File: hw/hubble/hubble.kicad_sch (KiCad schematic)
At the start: 36 parts

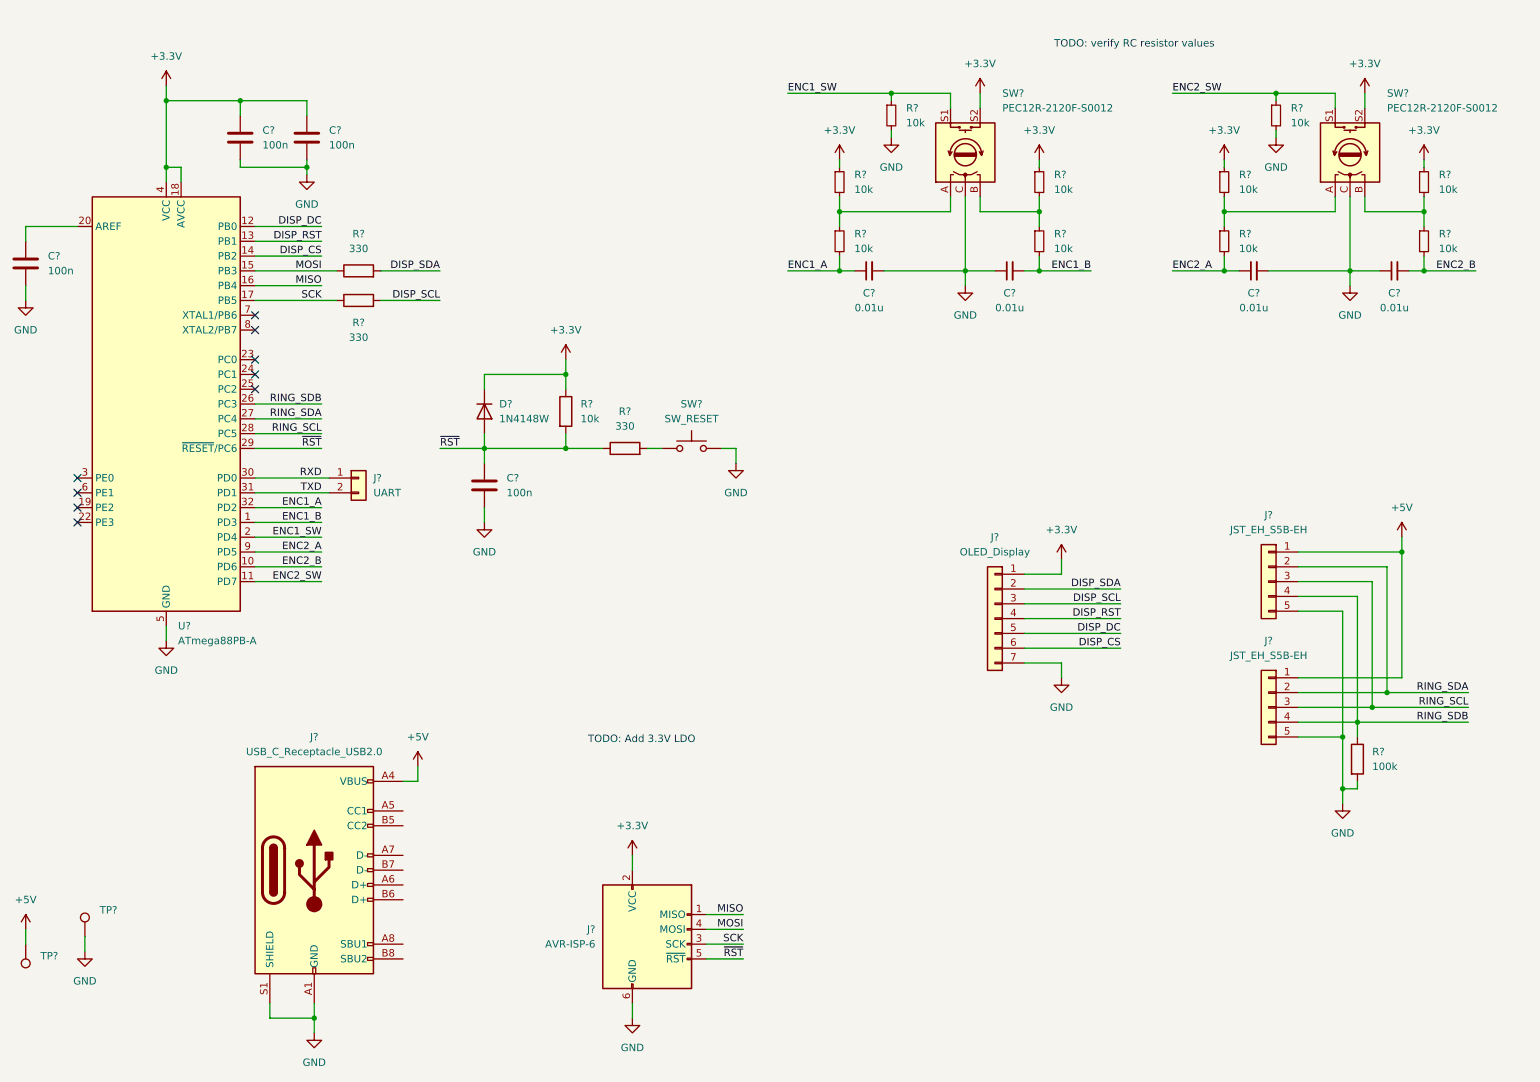
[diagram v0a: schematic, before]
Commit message: Switch to dc barrel jack, add some todos
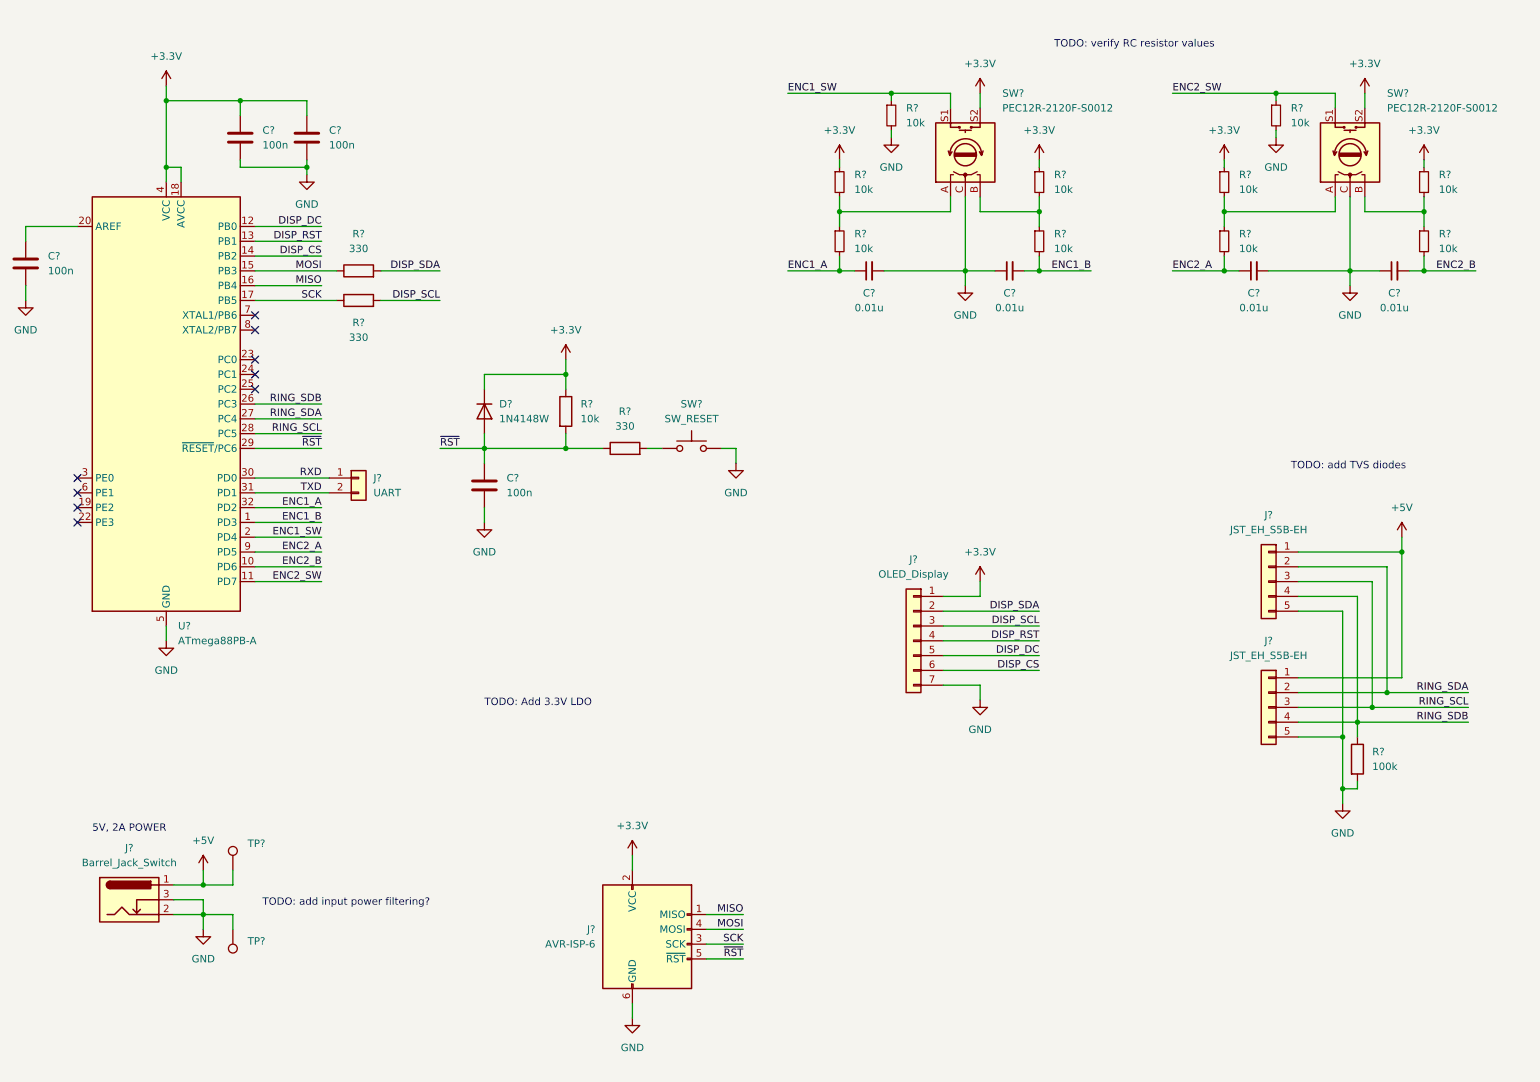
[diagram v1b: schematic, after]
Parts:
- removed J?: USB_C_Receptacle_USB2.0, Connector_USB:USB_C_Receptacle_GCT_USB4085, symbol Connector:USB_C_Receptacle_USB2.0
- removed TP? (x2): TestPoint, symbol Connector:TestPoint
- added J?: Barrel_Jack_Switch, Connector_BarrelJack:BarrelJack_Horizontal, symbol Connector:Barrel_Jack_Switch
- added TP? (x2): TestPoint, symbol Connector:TestPoint
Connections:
- net +5V: now also J?.1, TP?.1
- net GND: now also J?.2, J?.3, TP?.1
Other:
- note added: "5V, 2A POWER"
- note added: "TODO: add TVS diodes"
- note added: "TODO: add input power filtering?"
- moved on the sheet: J?

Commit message: Add 3.3V LDO
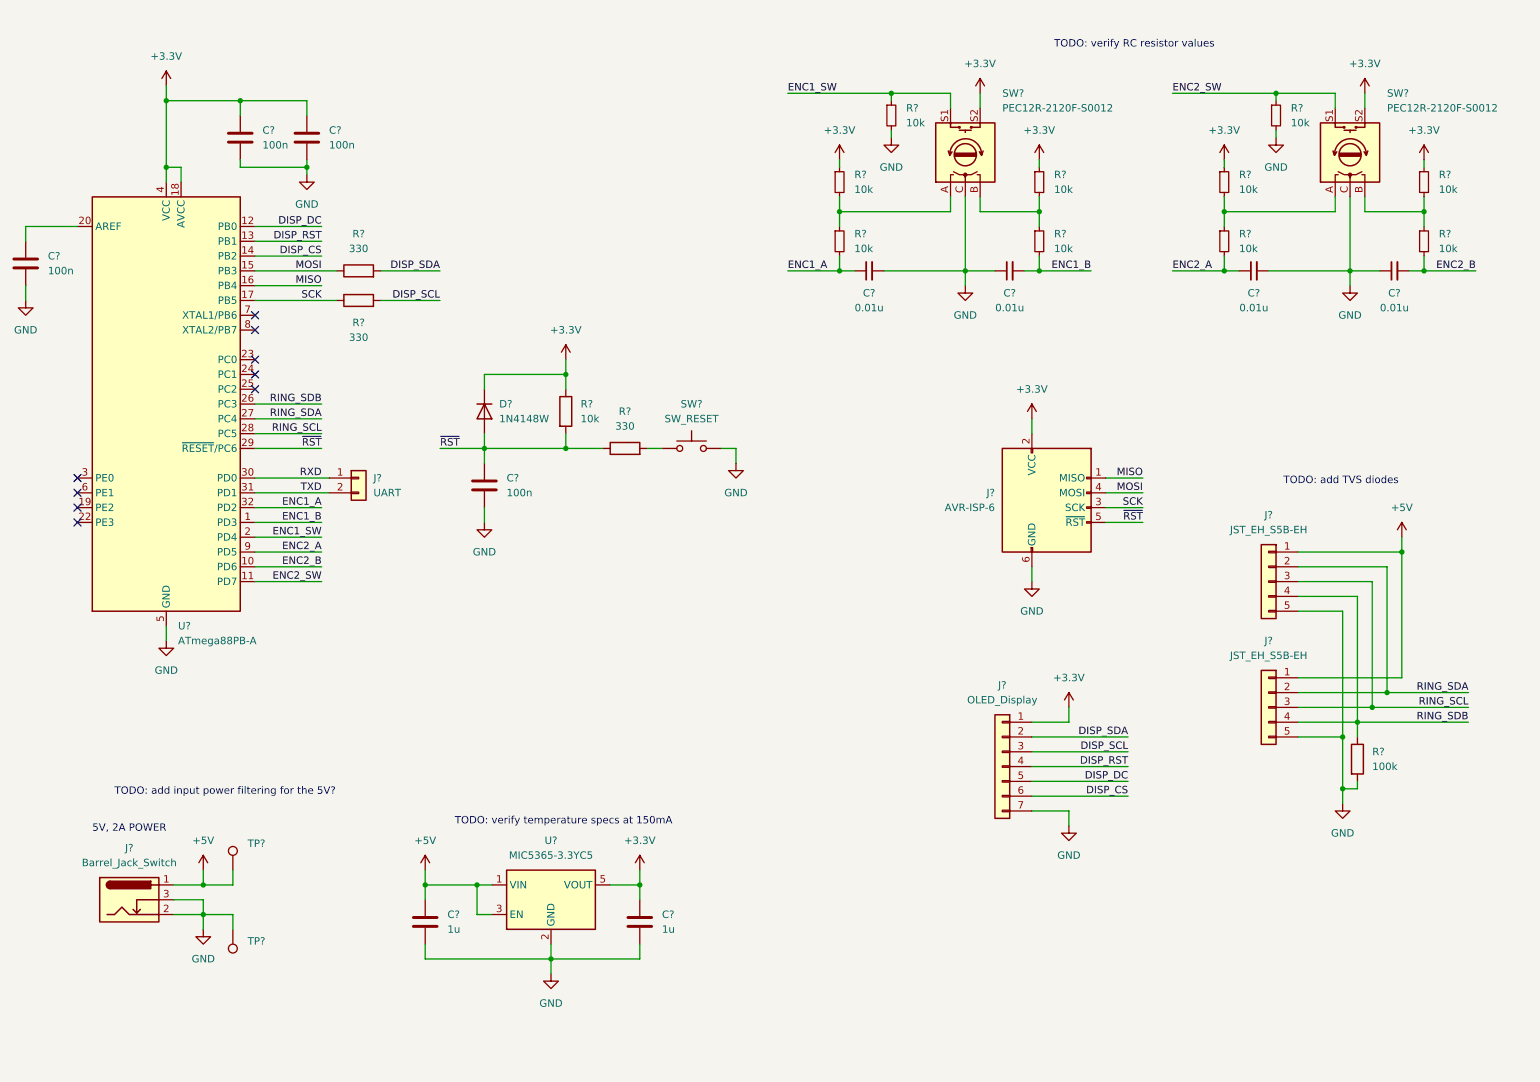
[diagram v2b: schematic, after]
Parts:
- added C? (x2): 1u, symbol Device:C
- added U?: MIC5365-3.3YC5, Package_TO_SOT_SMD:SOT-353_SC-70-5, symbol Regulator_Linear:MIC5365-3.3YC5
- SW?: footprint (none) -> Button_Switch_THT:SW_PUSH_6mm
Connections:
- net +3.3V: now also C?.1, U?.5 (VOUT)
- net +5V: now also C?.1, U?.1 (VIN), U?.3 (EN)
- net GND: now also C?.2, C?.2, U?.2 (GND)
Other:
- note added: "TODO: add input power filtering for the 5V?"
- note added: "TODO: verify temperature specs at 150mA"
- note removed: "TODO: Add 3.3V LDO"
- note removed: "TODO: add input power filtering?"
- moved on the sheet: J?

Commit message: Start initial hubble layout
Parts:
- added TP3: TestPoint, TestPoint:TestPoint_THTPad_D2.0mm_Drill1.0mm, symbol Connector:TestPoint
- added U3: DRTR5V0U4S-7, Package_TO_SOT_SMD:SOT-363_SC-70-6, symbol earendel:DRTR5V0U4S-7
- C10, C9: renamed from C?; footprint (none) -> Capacitor_SMD:C_0805_2012Metric
- R10, R3: renamed from R?; footprint (none) -> Resistor_SMD:R_0805_2012Metric
- SW1, SW2: renamed from SW?; footprint (none) -> earendel:PEC12R-2120F-S0012
- TP1, TP2: renamed from TP?; footprint (none) -> TestPoint:TestPoint_THTPad_D2.0mm_Drill1.0mm
- gave numbers to parts that had none: 31
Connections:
- net +3.3V: now also TP3.1
- net +5V: now also U3.5 (VDD)
- net GND: now also U3.2 (GND)
- net RING_SCL: now also U3.3 (CH_2)
- net RING_SDA: now also U3.1 (CH_1)
- net RING_SDB: now also U3.4 (CH_3)
- no-connect marks 9 -> 10
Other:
- note added: "5V, 2A Input"
- note added: "Encoders"
- note added: "ISP Header"
- note added: "MCU"
- note added: "OLED Header"
- note added: "Power"
- note added: "Ringlight Connectors"
- note removed: "5V, 2A POWER"
- note removed: "TODO: add TVS diodes"
- moved on the sheet: C1, C10, C2, C3, C4, C5, C6, C7, C8, C9, D1, J1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

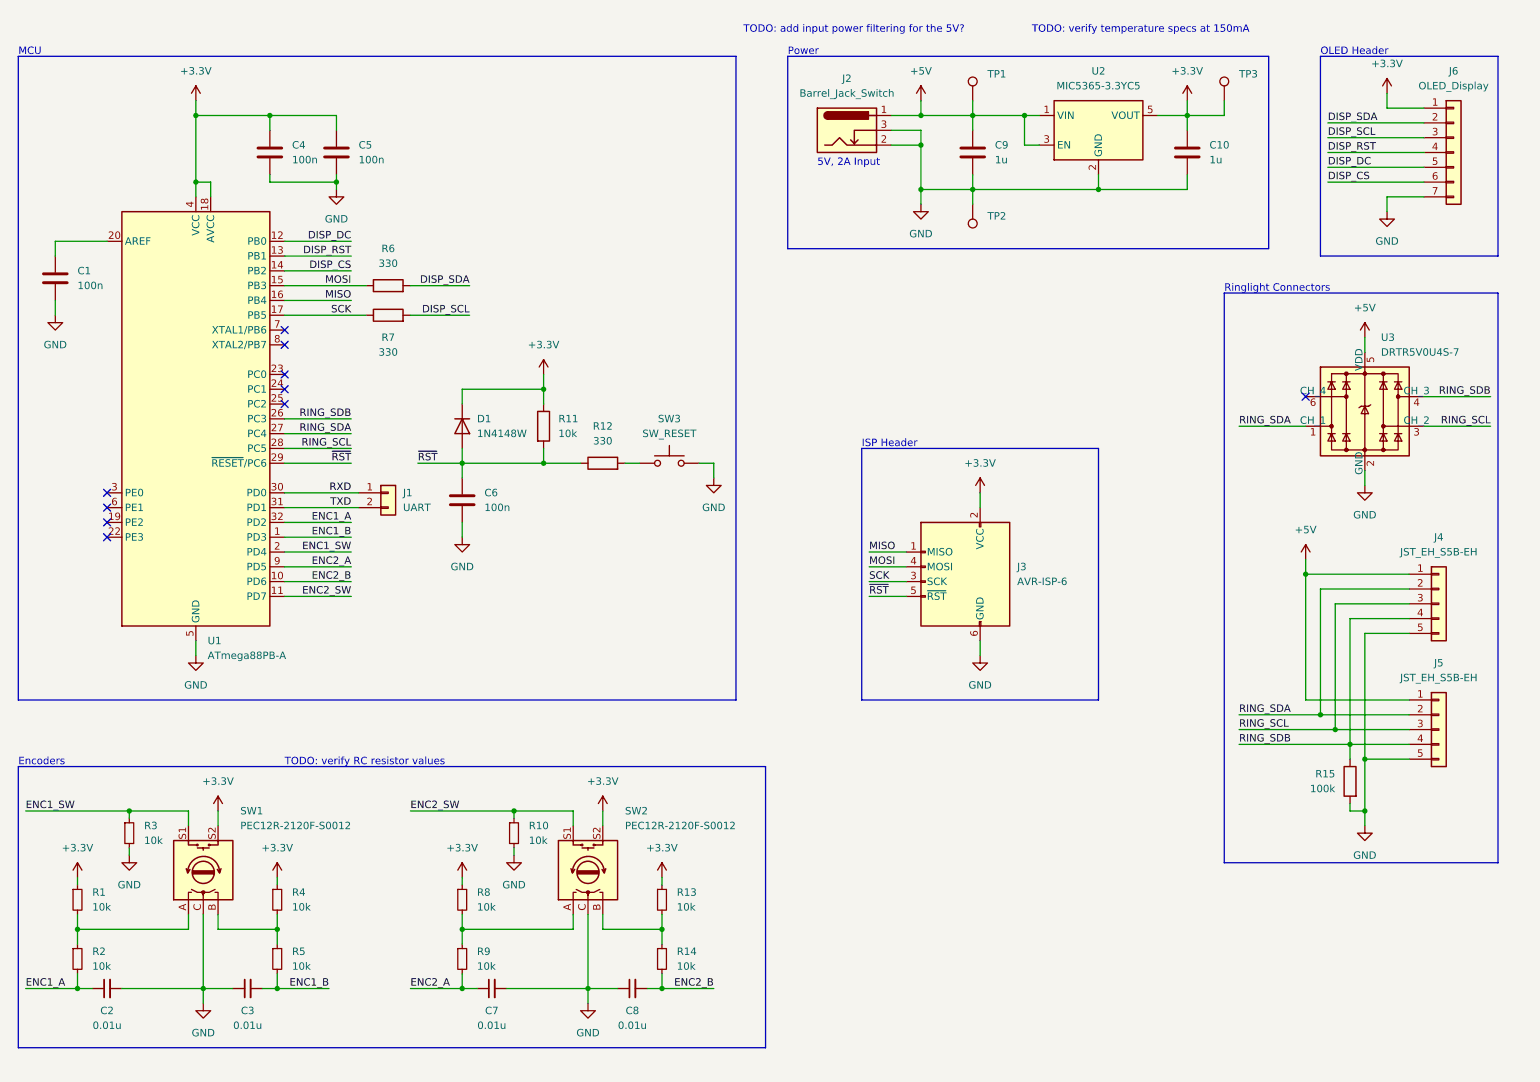
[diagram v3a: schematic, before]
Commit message: Add reverse polarity protection, more layout
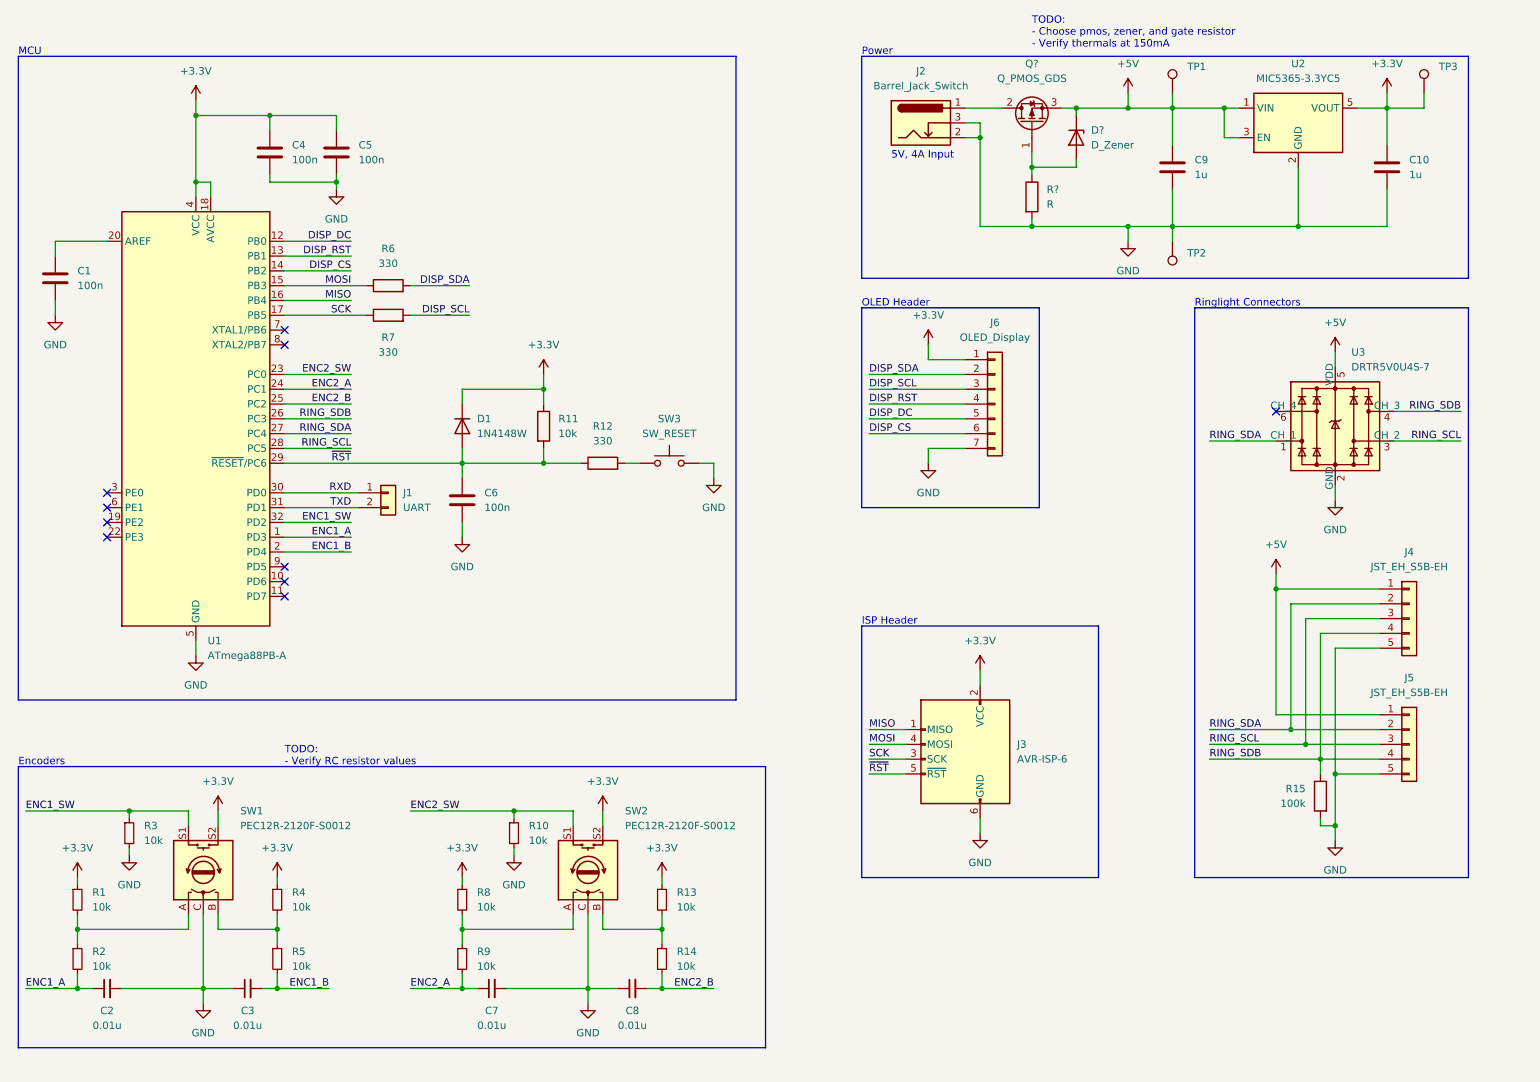
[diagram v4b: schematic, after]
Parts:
- added D?: D_Zener, symbol Device:D_Zener
- added Q?: Q_PMOS_GDS, symbol Device:Q_PMOS_GDS
- added R?: R, symbol Device:R
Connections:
- net +5V: now also D?.1 (K), Q?.3 (S); no longer J2.1
- net ENC1_A: now also U1.1 (PD3); no longer U1.32 (PD2)
- net ENC1_B: now also U1.2 (PD4); no longer U1.1 (PD3)
- net ENC1_SW: now also U1.32 (PD2); no longer U1.2 (PD4)
- net ENC2_A: now also U1.24 (PC1); no longer U1.9 (PD5)
- net ENC2_B: now also U1.25 (PC2); no longer U1.10 (PD6)
- net ENC2_SW: now also U1.23 (PC0); no longer U1.11 (PD7)
- net GND: now also R?.2
- new net: D?.2 (A), Q?.1 (G), R?.1
- new net: J2.1, Q?.2 (D)
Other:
- note added: "5V, 4A Input"
- note added: "TODO: - Choose pmos, zener, and gate resistor - Verify thermals at 150mA"
- note added: "TODO: - Verify RC resistor values"
- note removed: "5V, 2A Input"
- note removed: "TODO: add input power filtering for the 5V?"
- note removed: "TODO: verify RC resistor values"
- note removed: "TODO: verify temperature specs at 150mA"
- moved on the sheet: C10, C9, J2, J3, J4, J5, J6, R15, TP1, TP2, TP3, U2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
